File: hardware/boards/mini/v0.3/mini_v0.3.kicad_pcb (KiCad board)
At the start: 8 copper layers, 20 x 42 mm, 96 parts, among them IC1 NAU88C22YG, IC3 IS42S16160J-6BLI, J2 Top, J3 Bottom, U1 W25Q128JVP, U2 LTV-217-G, U4 STM32H750XBHx, Y1 Crystal_GND24, Y3 32.768kHz

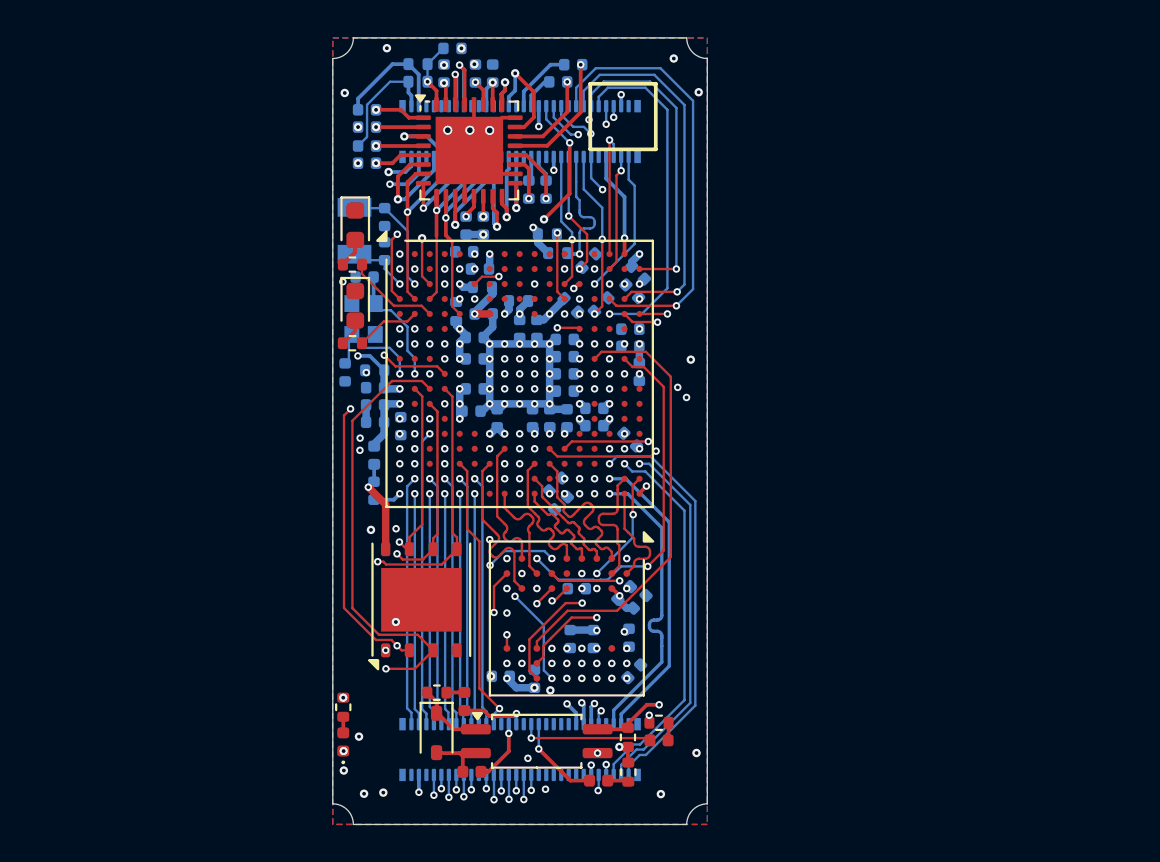
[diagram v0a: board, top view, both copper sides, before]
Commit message: mini: start routing single connector layout
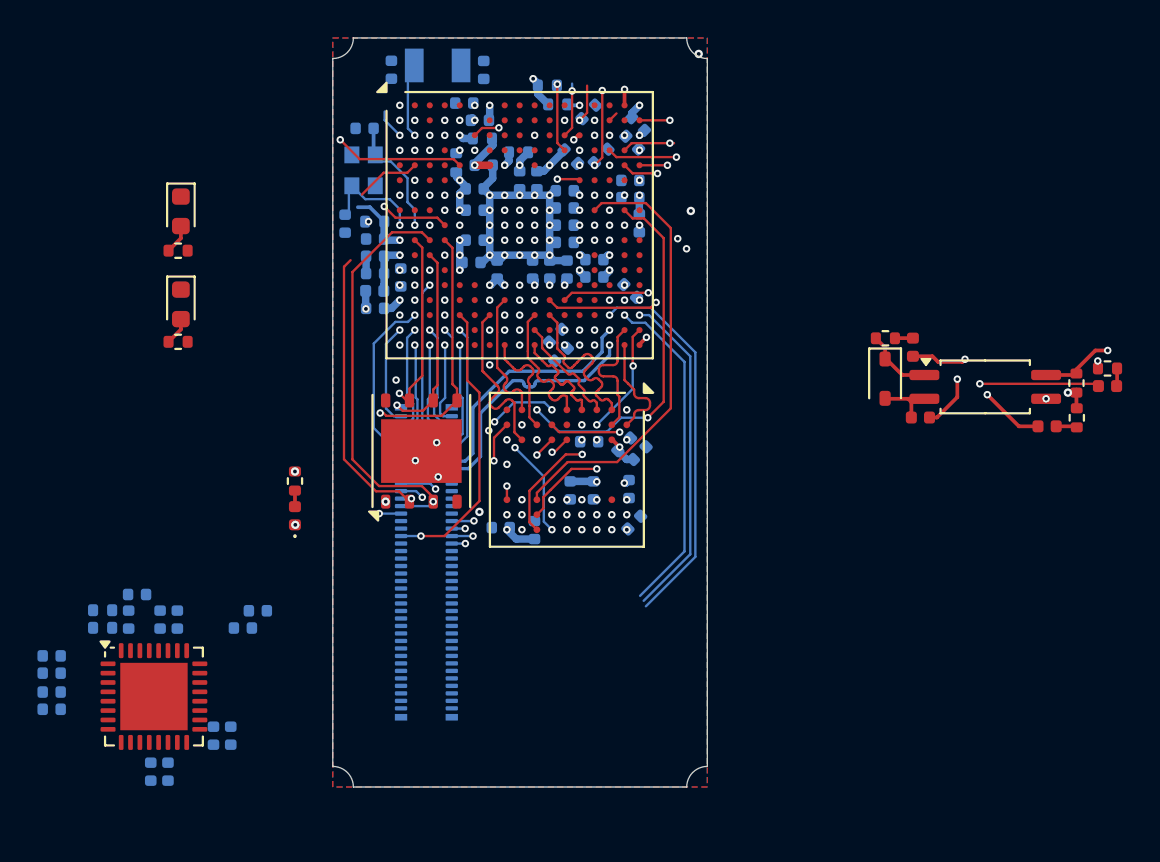
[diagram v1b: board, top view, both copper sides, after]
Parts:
- removed J2: Top, Connector_Hirose_DF40:Hirose_DF40C-60DP-0.4V_2x30-1MP_P0.4mm
- removed J3: Bottom, Connector_Hirose_DF40:Hirose_DF40C-60DP-0.4V_2x30-1MP_P0.4mm
- added J1: Connector, Connector_Hirose_DF40:Hirose_DF40C-80DP-0.4V_2x40-1MP_P0.4mm, B.Cu at (75.0, 85.0)
- moved C16 33.7 mm to (61.2, 96.2)
- moved C17 33.7 mm to (60.3, 96.2)
- moved C26 33.7 mm to (64.5, 94.3)
- moved C27 33.7 mm to (63.6, 94.3)
- moved C18 33.7 mm to (61.7, 88.1)
- moved C19 33.7 mm to (59.1, 88.1)
- moved C20 33.7 mm to (65.2, 88.5)
- moved C21 33.7 mm to (66.0, 87.6)
- moved C23 33.7 mm to (55.0, 90.9)
- moved C24 33.7 mm to (55.0, 91.9)
- moved C29 33.7 mm to (60.8, 88.1)
- moved IC1 33.7 mm to (60.5, 92.2)
- moved R4 33.7 mm to (57.7, 87.6)
- moved C22 33.7 mm to (55.0, 90.0)
- moved C25 33.7 mm to (55.0, 92.8)
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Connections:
- U4 pad R5: /PA7 -> /EXT_QSPI_DETECT
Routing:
- net /PH3: track 24.6 -> 0.00 mm, vias 2 -> 1
- net /PC2_C: track 22.3 -> 0.00 mm, vias 2 -> 1
- net /PC2: track 26.6 -> 4.47 mm, vias 3 -> 1
- net /PC1: track 24.2 -> 3.63 mm, vias 3 -> 1
- net /PA9: track 23.5 -> 3.86 mm
- net /SAI1_SD_A: track 11.7 -> 31.2 mm
- net /PA8: track 18.0 -> 0.00 mm
- net /SAI1_MCLK: track 10.5 -> 28.2 mm, vias 2 -> 1
- net /PH13: track 20.4 -> 3.02 mm
- net /QSPI_IO2: track 38.8 -> 22.4 mm, vias 2 -> 1
- net /SAI1_SD_B: track 10.0 -> 25.4 mm
- net /PA0: track 20.7 -> 5.47 mm, vias 2 -> 1
- net /PH14: track 16.6 -> 1.62 mm
- net /PA7: track 14.9 -> 0.00 mm, vias 1 -> 0
- net /SAI1_FS: track 11.5 -> 26.3 mm
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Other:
- board size 20 x 42 mm -> 20 x 40 mm

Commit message: mini: route SDMMC and SAI lines to near new connector
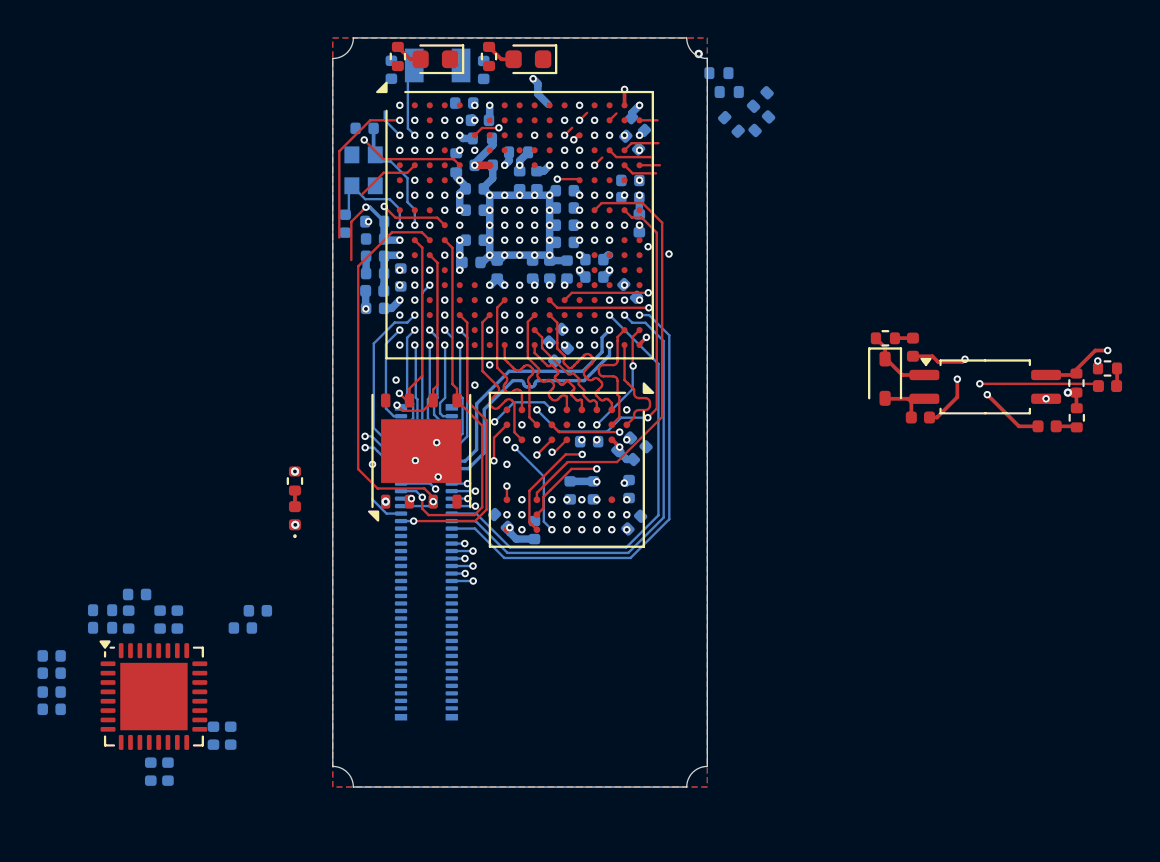
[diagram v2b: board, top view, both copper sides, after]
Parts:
- moved D2 20.3 mm to (80.4, 58.1), turned to 180 degrees
- moved R15 19.6 mm to (78.3, 58.0), turned to 90 degrees
- moved R17 19.2 mm to (73.5, 58.0), turned to 90 degrees
- moved D4 18.9 mm to (75.5, 58.1), turned to 180 degrees
- moved R10 9.18 mm to (90.6, 58.9)
- moved R13 9.18 mm to (91.2, 59.9)
- moved R14 9.18 mm to (92.8, 60.3)
- moved R11 8.75 mm to (91.3, 61.6)
- moved R12 8.75 mm to (92.9, 61.6)
- moved C9 0.36 mm to (79.0, 82.8), turned to 135 degrees
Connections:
- J1 pad 33: unconnected-(J1-Pin_33-Pad33) -> GND
- J1 pad 35: unconnected-(J1-Pin_35-Pad35) -> /SDMMC1_D2
- J1 pad 37: unconnected-(J1-Pin_37-Pad37) -> /SDMMC1_D3
- J1 pad 39: unconnected-(J1-Pin_39-Pad39) -> /SDMMC1_CK
- J1 pad 41: unconnected-(J1-Pin_41-Pad41) -> /SDMMC1_CMD
- J1 pad 43: unconnected-(J1-Pin_43-Pad43) -> /SDMMC1_D1
- J1 pad 45: /PB12 -> /SDMMC1_D0
- J1 pad 47: /PB13 -> GND
- J1 pad 48: /EXT_QSPI_DETECT -> unconnected-(J1-Pin_48-Pad48)
- J1 pad 49: /PH8 -> /PD13
- J1 pad 51: /PH7 -> /PD12
- J1 pad 52: unconnected-(J1-Pin_52-Pad52) -> /EXT_QSPI_DETECT
- J1 pad 53: unconnected-(J1-Pin_53-Pad53) -> /PD11
- J1 pad 55: unconnected-(J1-Pin_55-Pad55) -> /PB12
- J1 pad 57: unconnected-(J1-Pin_57-Pad57) -> /PB13
- J1 pad 59: unconnected-(J1-Pin_59-Pad59) -> /PH8
- J1 pad 61: unconnected-(J1-Pin_61-Pad61) -> /PH7
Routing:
- net /SDMMC1_D2: track 0.68 -> 44.0 mm, vias 1 -> 2
- net /SDMMC1_D3: track 2.01 -> 43.1 mm, vias 1 -> 2
- net /SDMMC1_CK: track 2.93 -> 43.4 mm, vias 1 -> 2
- net /SDMMC1_CMD: track 3.69 -> 39.8 mm, vias 1 -> 2
- net /SDMMC1_D0: track 3.05 -> 36.5 mm, vias 1 -> 2
- net /SDMMC1_D1: track 4.16 -> 37.4 mm
- net /EXT_QSPI_DETECT: track 43.5 -> 15.8 mm, vias 2 -> 1
- net /PD13: track 17.7 -> 25.0 mm
- net /PD12: track 17.7 -> 24.9 mm
- net /VBAT: track 1.47 -> 8.52 mm
- net /PD11: track 20.4 -> 24.3 mm
- net /RST: track 3.51 -> 6.23 mm, vias 1 -> 2
- net /DIN_MIDI_TX: track 21.8 -> 19.5 mm
- net unconnected-(J1-Pin_70-Pad70): track 0.00 -> 2.30 mm, vias 0 -> 1
- net unconnected-(J1-Pin_68-Pad68): track 0.00 -> 2.22 mm, vias 0 -> 1
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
